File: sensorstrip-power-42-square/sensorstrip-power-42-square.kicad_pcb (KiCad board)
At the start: 2 copper layers, 50 x 22 mm, 17 parts, among them J1 USB_C_Receptacle_PowerOnly, J2 Conn_01x02_MountingPin, J3 Conn_01x02_MountingPin, J4 Conn_01x02_MountingPin, J5 Conn_01x02_MountingPin, SW1 SW_DP3T

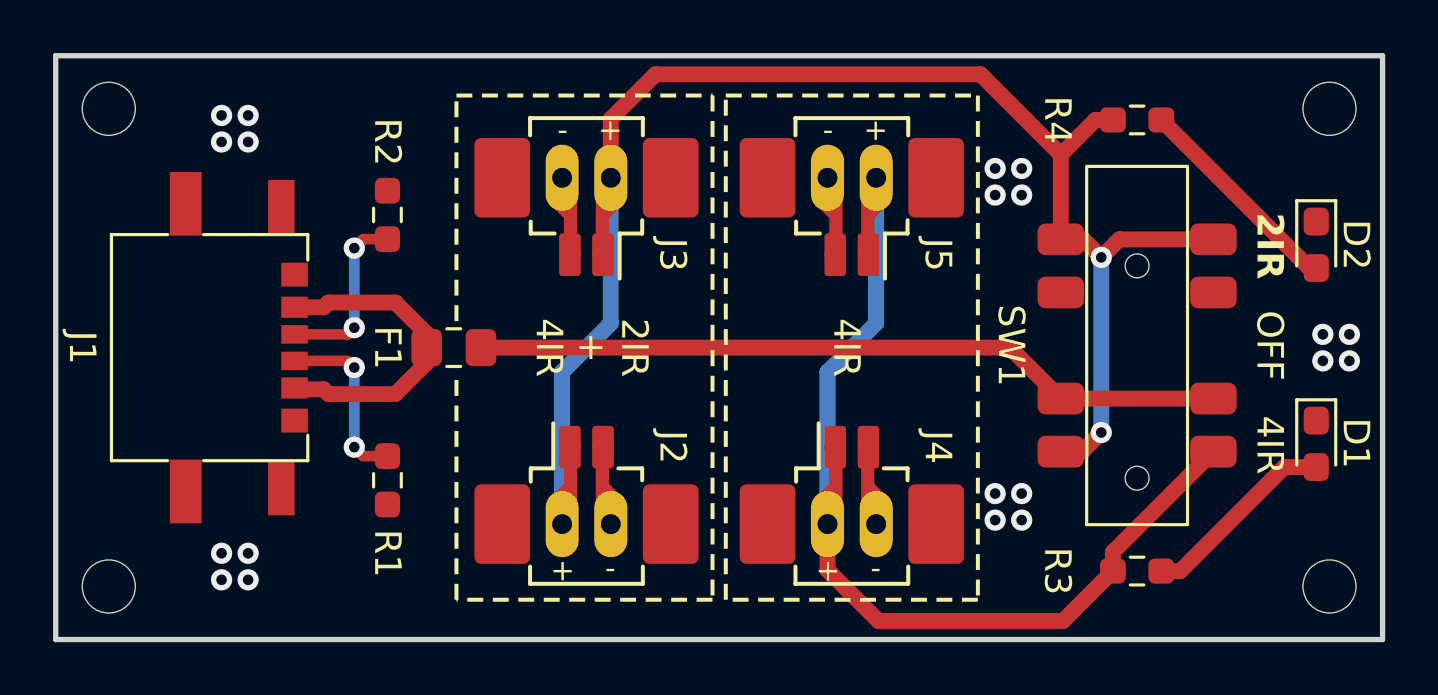
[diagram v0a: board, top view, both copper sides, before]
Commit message: Update 2/4IR square board for consistent status LED behaviour
Update DP3T switch footprint to make installing JS203011SCQN easier

Rename 2IR/4IR diamond layout board for clarity
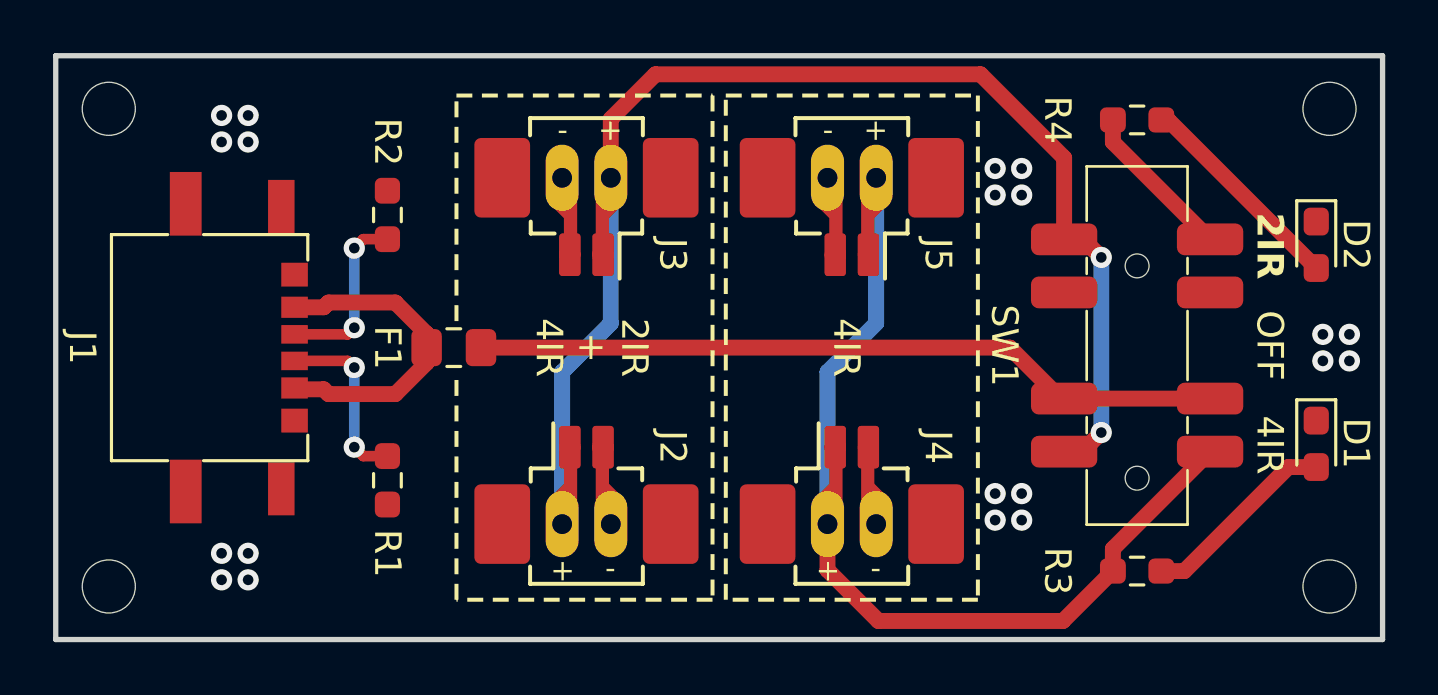
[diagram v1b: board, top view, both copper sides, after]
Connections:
- R4 pad 2: VCC_2IR -> Net-(R4-Pad2)
- SW1 pad 5: VCC_2IR -> Net-(R4-Pad2)
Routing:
- net VCC_2IR: track 55.4 -> 48.4 mm
- net Net-(R4-Pad2): track 0.00 -> 6.02 mm

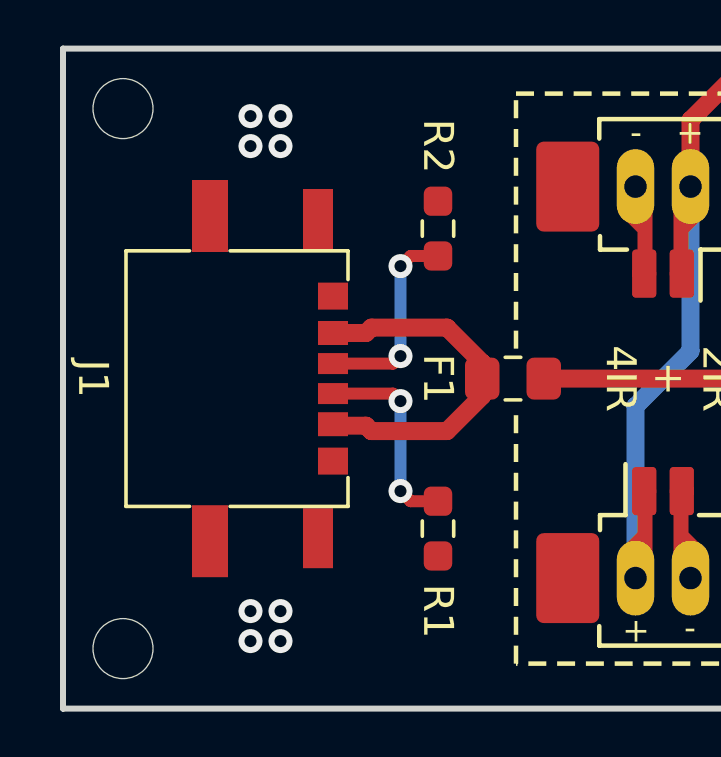
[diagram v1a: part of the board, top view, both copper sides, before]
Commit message: Update USB-C connector
Allowances for GCT USB4135-GF-A footprint
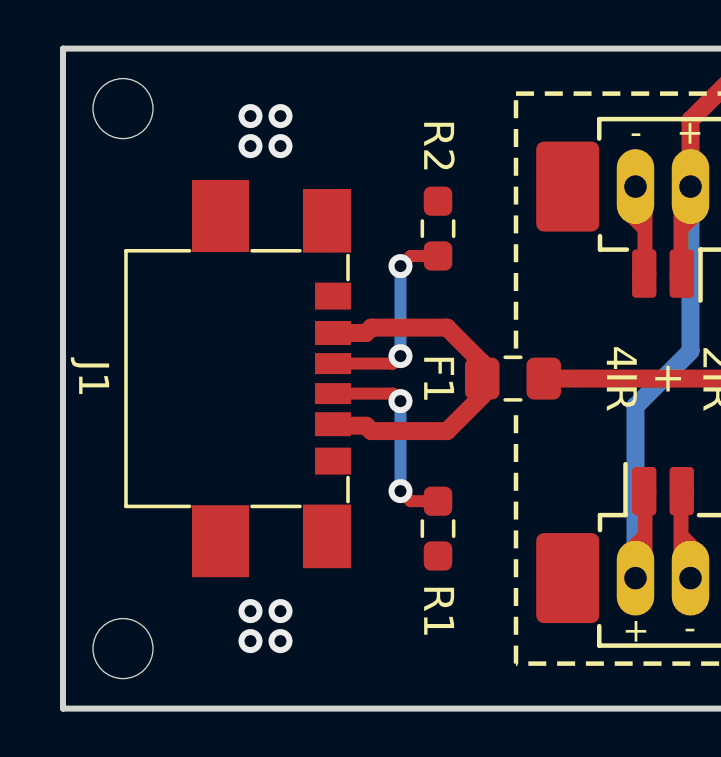
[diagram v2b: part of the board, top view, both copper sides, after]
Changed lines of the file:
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@@
 		)
 		(fp_line
-			(start 4.26 3.43)
-			(end 4.26 -0.5)
+			(start 4.26 2.7)
+			(end 4.26 1.1)
 			(stroke
 				(width 0.12)
@@
 		)
 		(fp_line
-			(start -4.26 -0.5)
-			(end -4.26 3.43)
+			(start -4.26 1.1)
+			(end -4.26 2.7)
 			(stroke
 				(width 0.12)
@@
 		(fp_line
 			(start -3.3 -0.5)
-			(end -4.25 -0.5)
+			(end -4.1 -0.5)
 			(stroke
 				(width 0.12)
@@
 		)
 		(fp_line
-			(start 4.26 -0.5)
+			(start 4.1 -0.5)
 			(end 3.3 -0.5)
 			(stroke
@@
 		(pad "A5" smd rect
 			(at -0.5 0 270)
-			(size 0.7 1)
+			(size 0.7 1.2)
 			(layers "F.Cu" "F.Paste" "F.Mask")
 			(net 2 "/CC1")
@@
 		(pad "A9" smd rect
 			(at 1.52 0 270)
-			(size 0.8 1)
+			(size 0.8 1.2)
 			(layers "F.Cu" "F.Paste" "F.Mask")
 			(net 4 "/VBUS")
@@
 		(pad "A12" smd rect
 			(at 2.75 0 270)
-			(size 0.9 1)
+			(size 0.9 1.2)
 			(layers "F.Cu" "F.Paste" "F.Mask")
 			(net 1 "GND")
@@
 		(pad "B5" smd rect
 			(at 0.5 0 270)
-			(size 0.7 1)
+			(size 0.7 1.2)
 			(layers "F.Cu" "F.Paste" "F.Mask")
 			(net 3 "/CC2")
@@
 		(pad "B9" smd rect
 			(at -1.52 0 270)
-			(size 0.8 1)
+			(size 0.8 1.2)
 			(layers "F.Cu" "F.Paste" "F.Mask")
 			(net 4 "/VBUS")
@@
 		(pad "B12" smd rect
 			(at -2.75 0 270)
-			(size 0.9 1)
+			(size 0.9 1.2)
 			(layers "F.Cu" "F.Paste" "F.Mask")
 			(net 1 "GND")
@@
 		)
 		(pad "S1" smd rect
-			(at -5.42 4.1 270)
-			(size 2.4 1.2)
+			(at -5.42 3.75 270)
+			(size 2.4 1.9)
 			(layers "F.Cu" "F.Paste" "F.Mask")
 			(net 1 "GND")
@@
 		)
 		(pad "S1" smd rect
-			(at -5.32 0.5 270)
-			(size 2 1)
+			(at -5.26 0.2 270)
+			(size 2.12 1.6)
 			(layers "F.Cu" "F.Paste" "F.Mask")
 			(net 1 "GND")
@@
 		)
 		(pad "S1" smd rect
-			(at 5.32 0.5 270)
-			(size 2 1)
+			(at 5.26 0.2 270)
+			(size 2.12 1.6)
 			(layers "F.Cu" "F.Paste" "F.Mask")
 			(net 1 "GND")
@@
 		)
 		(pad "S1" smd rect
-			(at 5.42 4.1 270)
-			(size 2.4 1.2)
+			(at 5.42 3.75 270)
+			(size 2.4 1.9)
 			(layers "F.Cu" "F.Paste" "F.Mask")
 			(net 1 "GND")
